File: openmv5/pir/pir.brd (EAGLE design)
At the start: 35.6 x 26.7 mm, 59 parts, among them IC1 AP3032KTR-G1, IC2 AP3032KTR-G1, J1 OPENMV5-TOP, Q1 2N7002KW_R1_00001, U1 EKMB1307113K, U2 MIC5365-3.3YMT-TZ

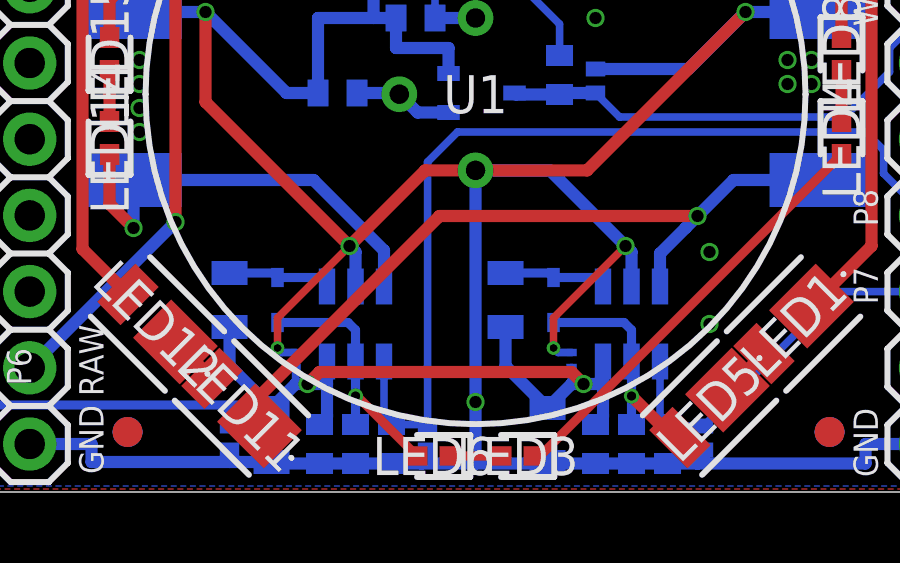
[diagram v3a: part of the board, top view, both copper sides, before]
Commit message: Remove 0201 caps
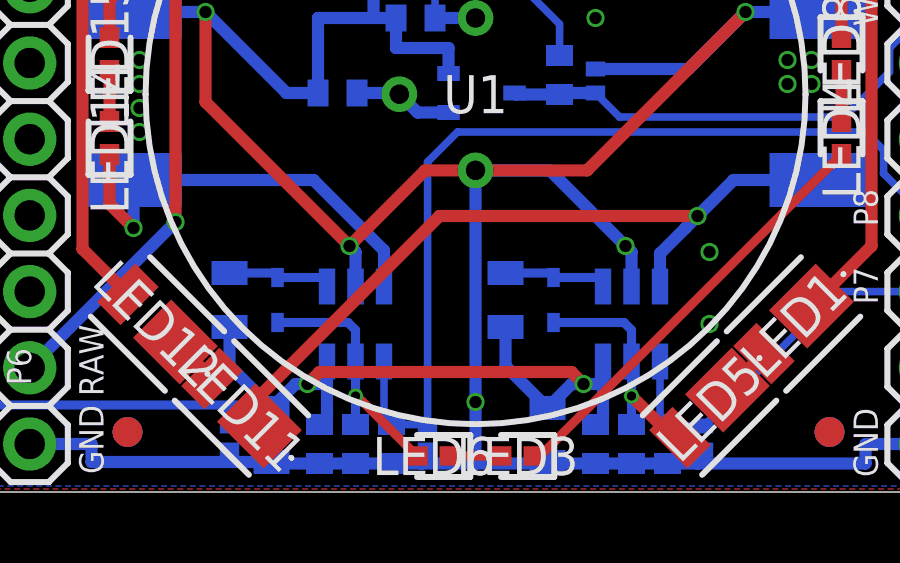
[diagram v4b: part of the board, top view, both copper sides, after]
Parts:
- removed C10, C9: 4.7uF, sfe:0402-CAP
- C3: value 0.22uF -> 1uF; device rcl:C0201 -> sfe:0402-CAP
- C4: value 1uF -> 22uF; device sfe:0402-CAP -> SparkFun-Capacitors:0805
- C5: value 22uF -> 4.7uF; device SparkFun-Capacitors:0805 -> sfe:0402-CAP
- C6: value 4.7uF -> 1uF
- C7: value 0.22uF -> 4.7uF; device rcl:C0201 -> sfe:0402-CAP
- C8: value 1uF -> 4.7uF
- moved C8 14.3 mm to (17.0, 15.8), turned to 180 degrees
- moved C7 13.5 mm to (15.6, 17.6)
- moved C4 12.0 mm to (12.2, 1.90)
- moved C3 3.44 mm to (24.2, 1.60)
- moved C5 1.63 mm to (13.8, 1.60)
- moved C6 1.20 mm to (15.0, 1.60)
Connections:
- net GND: now also C3.1, C7.1; no longer C10.1, C3.2, C7.2, C9.1
- net IOV: now also C6.2; no longer C8.2
- net RAW: now also C7.2; no longer C9.2
- net VCC: now also C4.2; no longer C3.1, C6.2, C7.1
- net VDD: now also C8.2; no longer C10.2
- net WOV: now also C3.2; no longer C4.2
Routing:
- net GND: track 116.2 -> 106.1 mm, vias 20 -> 18
- net VCC: track 39.2 -> 38.1 mm
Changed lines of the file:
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@@
 <attribute name="VALUE" x="15.4795" y="12.157" size="0.4064" layer="28" rot="MR0"/>
 </element>
-<element name="C10" library="sfe" package="0402-CAP" value="4.7uF" x="17" y="15.8" smashed="yes" rot="MR180">
+<element name="C8" library="sfe" package="0402-CAP" value="4.7uF" x="17" y="15.8" smashed="yes" rot="MR180">
 <attribute name="MPN" value="JMK105BBJ475MV-F" x="11" y="6.6" size="1.778" layer="28" rot="MR180" display="off"/>
 <attribute name="NAME" x="16.111" y="15.1015" size="0.4064" layer="26" rot="MR180"/>
 <attribute name="VALUE" x="15.9205" y="16.943" size="0.4064" layer="28" rot="MR180"/>
 </element>
-<element name="C9" library="sfe" package="0402-CAP" value="4.7uF" x="15.6" y="17.6" smashed="yes" rot="MR90">
+<element name="C7" library="sfe" package="0402-CAP" value="4.7uF" x="15.6" y="17.6" smashed="yes" rot="MR90">
 <attribute name="MPN" value="JMK105BBJ475MV-F" x="24.8" y="11.2" size="1.778" layer="28" rot="MR90" display="off"/>
 <attribute name="NAME" x="16.2985" y="16.711" size="0.4064" layer="26" rot="MR90"/>
@@
 <attribute name="VALUE" x="20.511" y="1.9" size="0.6096" layer="28" font="vector" ratio="20" rot="MR90" align="top-center"/>
 </element>
-<element name="C3" library="rcl" library_urn="urn:adsk.eagle:library:334" package="C0201" package3d_urn="urn:adsk.eagle:package:23690/2" value="0.22uF" x="22.2" y="4.4" smashed="yes" rot="MR90">
-<attribute name="MPN" value="GRM033R60J224ME15D" x="22.2" y="4.4" size="1.778" layer="28" rot="MR90" display="off"/>
-<attribute name="NAME" x="22.835" y="3.765" size="1.27" layer="26" rot="MR90"/>
-<attribute name="POPULARITY" value="0" x="22.2" y="4.4" size="1.778" layer="28" rot="MR90" display="off"/>
-<attribute name="SPICEPREFIX" value="C" x="22.2" y="4.4" size="1.778" layer="28" rot="MR90" display="off"/>
-<attribute name="VALUE" x="20.295" y="3.765" size="1.27" layer="28" rot="MR90"/>
-</element>
 <element name="C2" library="sfe" package="0402-CAP" value="4.7uF" x="23" y="1.6" smashed="yes" rot="MR90">
 <attribute name="MPN" value="JMK105BBJ475MV-F" x="26.6" y="-1.6" size="1.778" layer="28" rot="MR90" display="off"/>
@@
 <attribute name="VALUE" x="21.857" y="0.5205" size="0.4064" layer="28" rot="MR90"/>
 </element>
-<element name="C4" library="sfe" package="0402-CAP" value="1uF" x="24.2" y="1.6" smashed="yes" rot="MR90">
+<element name="C3" library="sfe" package="0402-CAP" value="1uF" x="24.2" y="1.6" smashed="yes" rot="MR90">
 <attribute name="MPN" value="GRM155R61H105KE05D" x="24.2" y="1.6" size="1.778" layer="28" rot="MR90" display="off"/>
 <attribute name="NAME" x="24.8985" y="0.711" size="0.4064" layer="26" rot="MR90"/>
@@
 <attribute name="VALUE" x="17.4" y="1.8" size="1.27" layer="28" rot="MR270" align="center"/>
 </element>
-<element name="C5" library="SparkFun-Capacitors" library_urn="urn:adsk.eagle:library:510" package="0805" package3d_urn="urn:adsk.eagle:package:37429/1" value="22uF" x="12.2" y="1.9" smashed="yes" rot="MR90">
+<element name="C4" library="SparkFun-Capacitors" library_urn="urn:adsk.eagle:library:510" package="0805" package3d_urn="urn:adsk.eagle:package:37429/1" value="22uF" x="12.2" y="1.9" smashed="yes" rot="MR90">
 <attribute name="MPN" value="CL21A226MQQNNNE" x="48.6" y="-24.5" size="1.778" layer="28" rot="MR90" display="off"/>
 <attribute name="NAME" x="13.089" y="1.9" size="0.6096" layer="26" font="vector" ratio="20" rot="MR90" align="bottom-center"/>
@@
 <attribute name="VALUE" x="11.311" y="1.9" size="0.6096" layer="28" font="vector" ratio="20" rot="MR90" align="top-center"/>
 </element>
-<element name="C7" library="rcl" library_urn="urn:adsk.eagle:library:334" package="C0201" package3d_urn="urn:adsk.eagle:package:23690/2" value="0.22uF" x="13" y="4.4" smashed="yes" rot="MR90">
-<attribute name="MPN" value="GRM033R60J224ME15D" x="40.6" y="-40.8" size="1.778" layer="28" rot="MR90" display="off"/>
-<attribute name="NAME" x="13.635" y="3.765" size="1.27" layer="26" rot="MR90"/>
-<attribute name="POPULARITY" value="0" x="40.6" y="-40.8" size="1.778" layer="28" rot="MR90" display="off"/>
-<attribute name="SPICEPREFIX" value="C" x="40.6" y="-40.8" size="1.778" layer="28" rot="MR90" display="off"/>
-<attribute name="VALUE" x="11.095" y="3.765" size="1.27" layer="28" rot="MR90"/>
-</element>
-<element name="C6" library="sfe" package="0402-CAP" value="4.7uF" x="13.8" y="1.6" smashed="yes" rot="MR90">
+<element name="C5" library="sfe" package="0402-CAP" value="4.7uF" x="13.8" y="1.6" smashed="yes" rot="MR90">
 <attribute name="MPN" value="JMK105BBJ475MV-F" x="45" y="-34.8" size="1.778" layer="28" rot="MR90" display="off"/>
 <attribute name="NAME" x="14.4985" y="0.711" size="0.4064" layer="26" rot="MR90"/>
 <attribute name="VALUE" x="12.657" y="0.5205" size="0.4064" layer="28" rot="MR90"/>
 </element>
-<element name="C8" library="sfe" package="0402-CAP" value="1uF" x="15" y="1.6" smashed="yes" rot="MR90">
+<element name="C6" library="sfe" package="0402-CAP" value="1uF" x="15" y="1.6" smashed="yes" rot="MR90">
 <attribute name="MPN" value="GRM155R61H105KE05D" x="46.2" y="-40.8" size="1.778" layer="28" rot="MR90" display="off"/>
 <attribute name="NAME" x="15.6985" y="0.711" size="0.4064" layer="26" rot="MR90"/>
@@
 <vertex x="0.1" y="26.7"/>
 </polygon>
-<contactref element="C9" pad="1"/>
-<contactref element="C10" pad="1"/>
+<contactref element="C7" pad="1"/>
+<contactref element="C8" pad="1"/>
 <contactref element="U2" pad="2"/>
 <contactref element="U2" pad="EP"/>
@@
 <contactref element="C1" pad="1"/>
 <contactref element="C2" pad="1"/>
-<contactref element="C3" pad="2"/>
 <contactref element="D5" pad="2"/>
-<contactref element="C4" pad="1"/>
+<contactref element="C3" pad="1"/>
 <contactref element="R2" pad="1"/>
 <contactref element="IC1" pad="2"/>
 <contactref element="R3" pad="2"/>
 <contactref element="D4" pad="2"/>
+<contactref element="C4" pad="1"/>
 <contactref element="C5" pad="1"/>
 <contactref element="C6" pad="1"/>
-<contactref element="C7" pad="2"/>
-<contactref element="C8" pad="1"/>
 <contactref element="R4" pad="1"/>
 <contactref element="IC2" pad="2"/>
-<wire x1="13" y1="4.65" x2="12.55" y2="4.65" width="0.254" layer="16"/>
-<wire x1="12.55" y1="4.65" x2="12.4" y2="4.8" width="0.254" layer="16"/>
-<via x="12.4" y="4.8" extent="1-16" drill="0.254"/>
 <wire x1="4.14" y1="1.6" x2="6.2" y2="1.6" width="0.4064" layer="16"/>
 <wire x1="6.2" y1="1.6" x2="6.2" y2="1" width="0.4064" layer="16"/>
@@
 <wire x1="21.4" y1="1" x2="21.55" y2="1" width="0.4064" layer="16"/>
 <wire x1="21.55" y1="1" x2="21.6" y2="0.95" width="0.4064" layer="16"/>
-<wire x1="22.2" y1="4.65" x2="21.75" y2="4.65" width="0.254" layer="16"/>
-<wire x1="21.75" y1="4.65" x2="21.6" y2="4.8" width="0.254" layer="16"/>
-<via x="21.6" y="4.8" extent="1-16" drill="0.254"/>
 <wire x1="19" y1="10.72" x2="19" y2="0.95" width="0.4064" layer="16"/>
 <wire x1="13.8" y1="0.95" x2="12.25" y2="0.95" width="0.4064" layer="16"/>
@@
 <wire x1="21.48" y1="10.72" x2="24" y2="8.2" width="0.4064" layer="16"/>
 <wire x1="24" y1="8.2" x2="24.2" y2="8" width="0.4064" layer="16"/>
-<wire x1="14.8" y1="8.2" x2="12.4" y2="5.8" width="0.254" layer="1"/>
-<wire x1="12.4" y1="5.8" x2="12.4" y2="4.8" width="0.254" layer="1"/>
 <via x="24" y="8.2" extent="1-16" drill="0.4064"/>
-<wire x1="21.6" y1="4.8" x2="21.6" y2="5.8" width="0.254" layer="1"/>
-<wire x1="21.6" y1="5.8" x2="24" y2="8.2" width="0.254" layer="1"/>
 <wire x1="7.6" y1="16" x2="10" y2="16" width="0.4064" layer="16"/>
 <via x="10" y="16" extent="1-16" drill="0.4064"/>
@@
 </signal>
 <signal name="RAW" class="3">
-<contactref element="C9" pad="2"/>
+<contactref element="C7" pad="2"/>
 <contactref element="U2" pad="4"/>
 <contactref element="U2" pad="3"/>
@@
 </signal>
 <signal name="VDD" class="3">
-<contactref element="C10" pad="2"/>
+<contactref element="C8" pad="2"/>
 <contactref element="U2" pad="1"/>
 <contactref element="U1" pad="1"/>
@@
 <contactref element="C1" pad="2"/>
 <contactref element="C2" pad="2"/>
-<contactref element="C3" pad="1"/>
 <contactref element="L1" pad="1"/>
 <contactref element="D5" pad="1"/>
 <contactref element="IC2" pad="6"/>
+<contactref element="C4" pad="2"/>
 <contactref element="C5" pad="2"/>
-<contactref element="C6" pad="2"/>
-<contactref element="C7" pad="1"/>
 <contactref element="L2" pad="1"/>
 <wire x1="14.05" y1="4.35" x2="14.05" y2="3.6" width="0.4064" layer="16"/>
@@
 <via x="22.6" y="3.6" extent="1-16" drill="0.4064"/>
 <wire x1="13.8" y1="4" x2="22.2" y2="4" width="0.4064" layer="1"/>
-<wire x1="13" y1="4.15" x2="13" y2="3.6" width="0.254" layer="16"/>
-<wire x1="22.2" y1="4.15" x2="22.2" y2="3.6" width="0.254" layer="16"/>
 <wire x1="12.2" y1="2.8" x2="10.8" y2="2.8" width="0.4064" layer="16"/>
 <wire x1="10.8" y1="2.8" x2="10.8" y2="2.2" width="0.4064" layer="16"/>
@@
 <contactref element="IC1" pad="5"/>
 <contactref element="D1" pad="1"/>
-<contactref element="C4" pad="2"/>
+<contactref element="C3" pad="2"/>
 <contactref element="LED5" pad="2"/>
 <wire x1="24.2" y1="4.35" x2="24.2" y2="3.2" width="0.3048" layer="16"/>
@@
 <contactref element="IC2" pad="5"/>
 <contactref element="D2" pad="1"/>
-<contactref element="C8" pad="2"/>
+<contactref element="C6" pad="2"/>
 <contactref element="LED6" pad="2"/>
 <wire x1="12.4" y1="5.65" x2="14.75" y2="5.65" width="0.3048" layer="16"/>
